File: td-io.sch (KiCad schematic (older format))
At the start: 99 parts, among them J1 USB_A, J2 USB_B, J3 JAMMA_Edge, J4 Conn_Coaxial, J5 DB15_Female_HighDensity, J6 Conn_02x04_Top_Bottom, J7 Conn_02x17_Odd_Even, J8 Conn_Coaxial, Q1 FDS6930B, Q2 FDS6930B, Q3 FDS6930B, SW1 SW_DIP_x02, U1 LM4950TS, U10 Pico, U11 TL081, U12 CPC1017N, U2 SP3481CN, U3 AD813, U4 74LS86, U5 AT24CS01-SSHM, U6 74LV166, U7 TPS568230, U8 74LV166, U9 74LV166

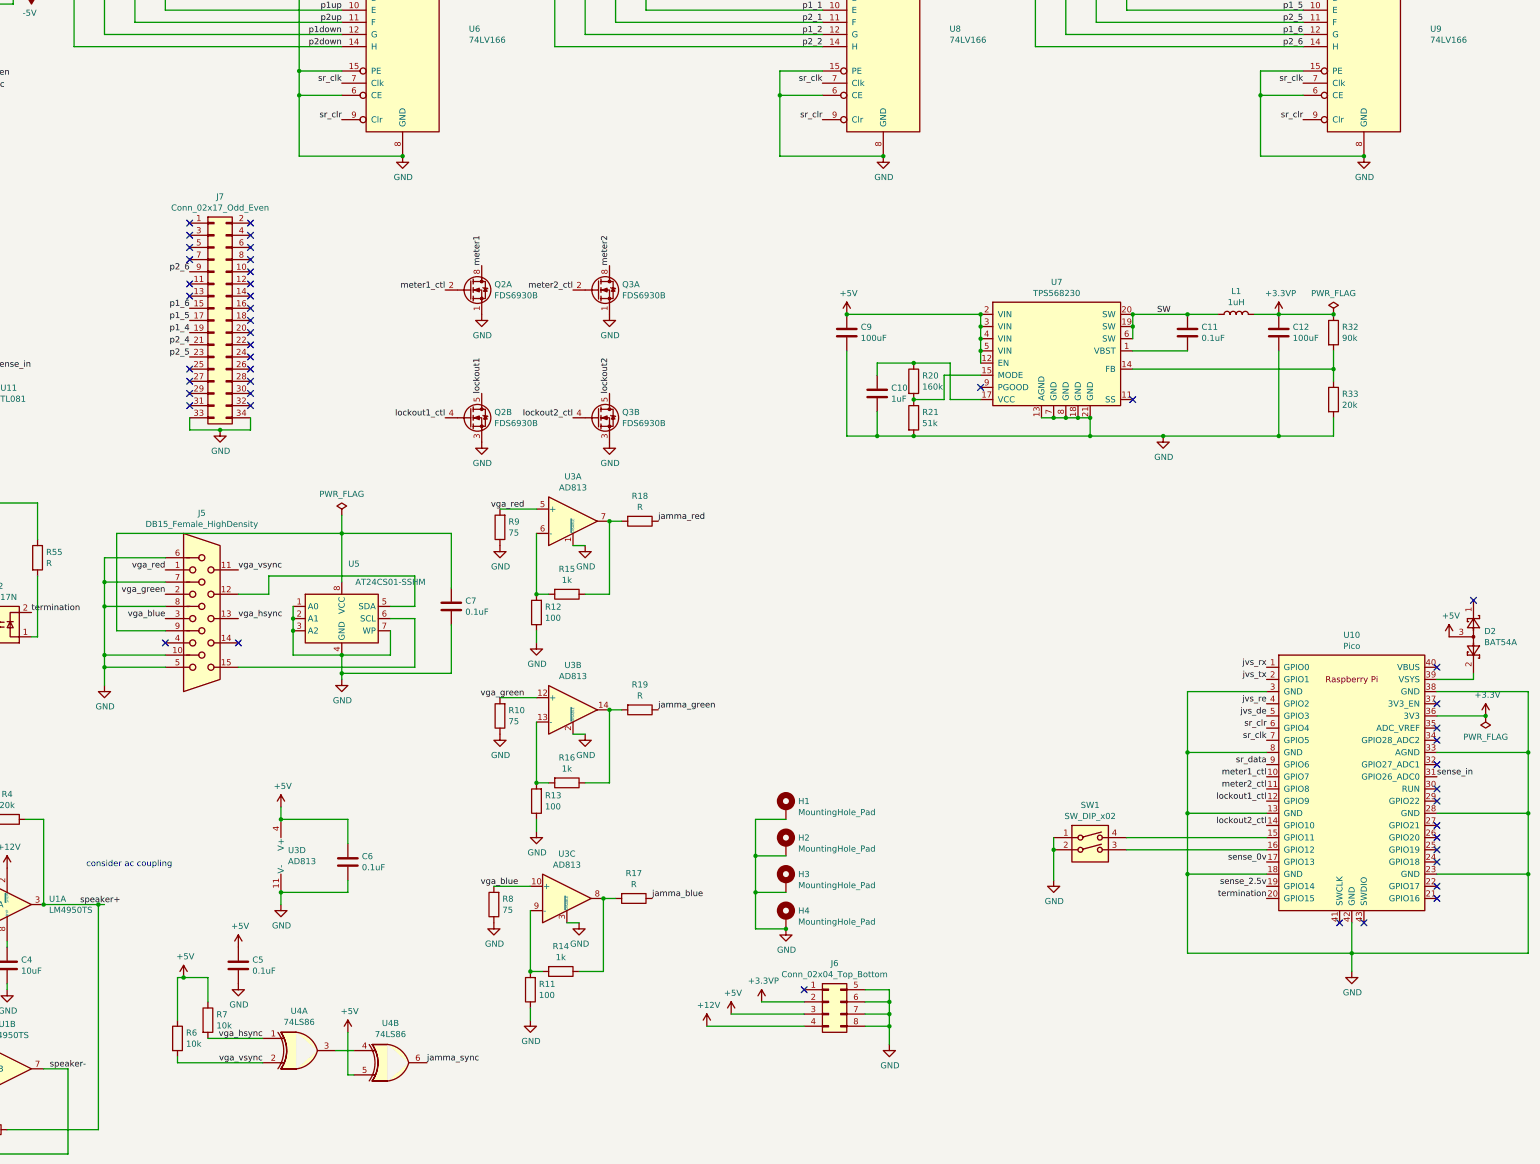
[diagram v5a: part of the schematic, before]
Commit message: More layout fixes
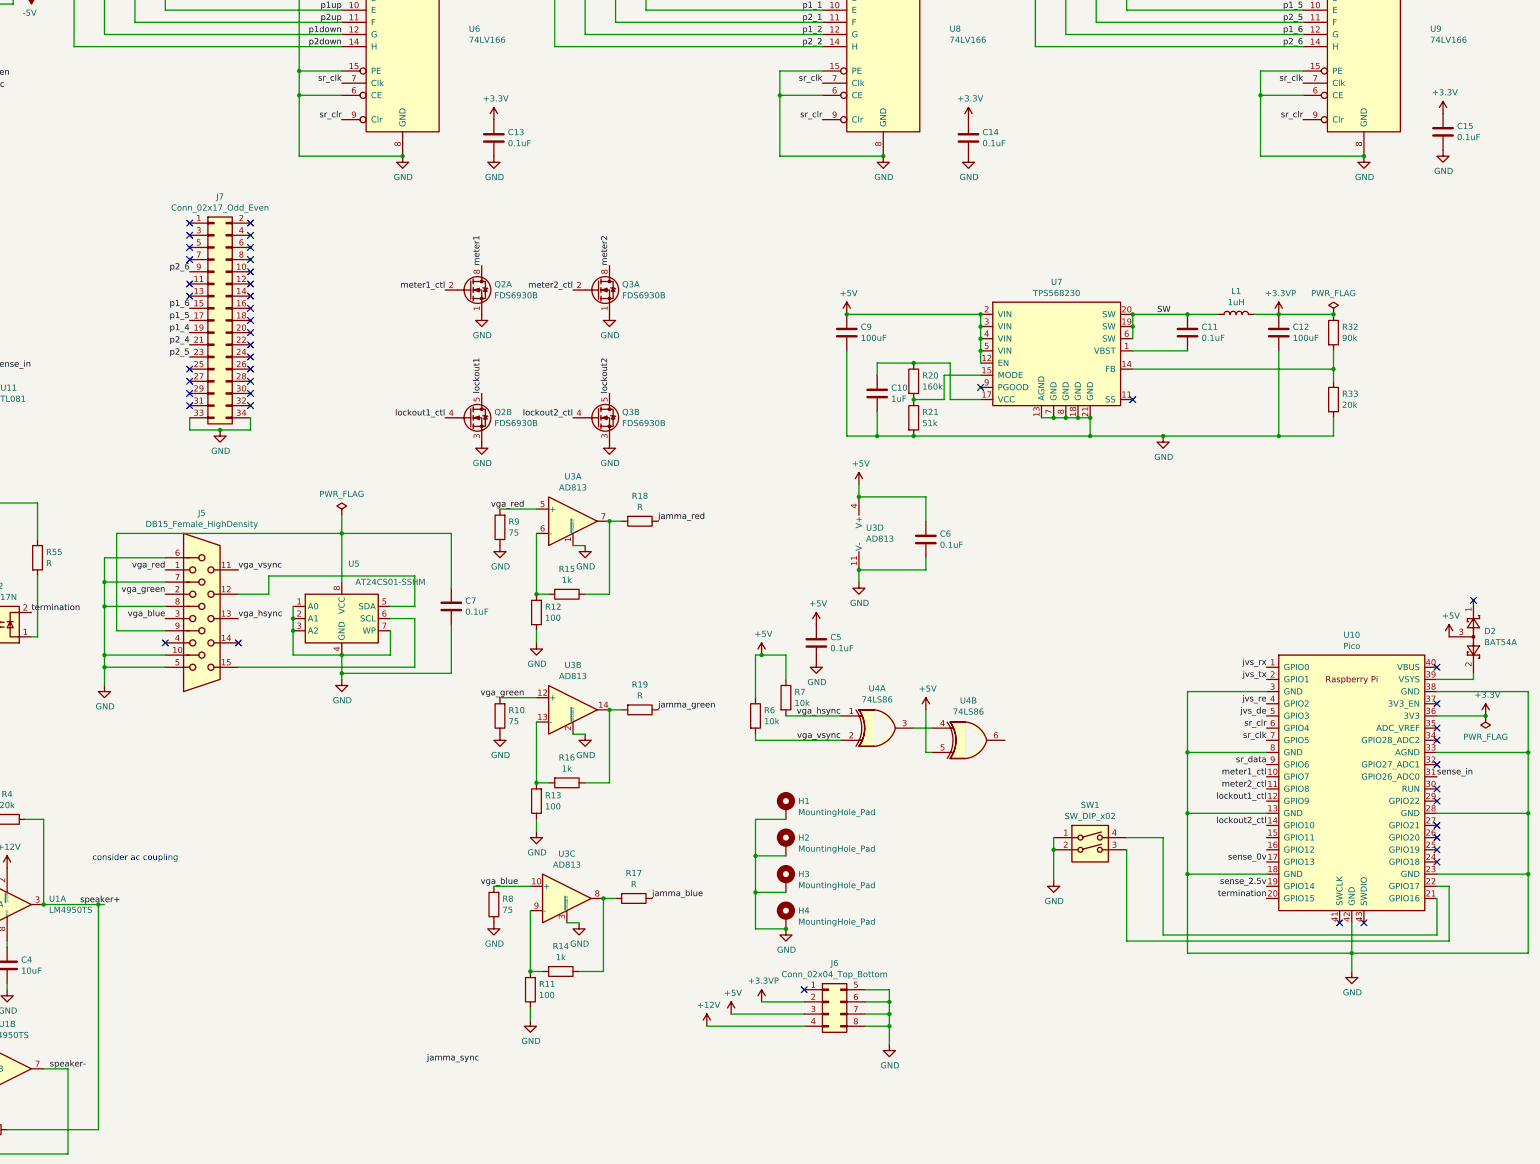
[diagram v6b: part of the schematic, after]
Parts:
- added C13, C14, C15: 0.1uF, Capacitor_SMD:C_0805_2012Metric, symbol Device:C
- R50, R51, R52, R53, R54, R55: footprint (none) -> Resistor_SMD:R_0805_2012Metric
- U11: footprint (none) -> Package_SO:SOIC-8_3.9x4.9mm_P1.27mm
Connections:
- net +3V3: now also C13.1, C14.1, C15.1
- net GND: now also C13.2, C14.2, C15.2
- net jamma_sync: no longer U4.6
- net at U10.15 (GPIO11): no longer SW1.4
- net at U10.16 (GPIO12): no longer SW1.3
- net at U10.21 (GPIO16): now also SW1.4
- net at U10.22 (GPIO17): now also SW1.3
- no-connect marks 53 -> 51
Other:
- moved on the sheet: C5, C6, R6, R7, U3D, U4A, U4B

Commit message: Switch from 74lv166 to 74lv165
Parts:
- U6, U8, U9: value 74LV166 -> 74LS165; symbol 74xx:74LS166 -> 74xx:74LS165
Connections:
- net GND: now also U6.10 (DS); no longer U6.1 (Ds), U6.6 (CE), U8.6 (CE), U9.6 (CE)
- net c1: now also U6.11 (D0); no longer U6.2 (A)
- net c2: now also U6.12 (D1); no longer U6.3 (B)
- net p1_1: now also U8.3 (D4); no longer U8.10 (E)
- net p1_2: now also U8.5 (D6); no longer U8.12 (G)
- net p1_3: now also U9.11 (D0); no longer U9.2 (A)
- net p1_4: now also U9.13 (D2); no longer U9.4 (C)
- net p1_5: now also U9.3 (D4); no longer U9.10 (E)
- net p1_6: now also U9.5 (D6); no longer U9.12 (G)
- net p1down: now also U6.5 (D6); no longer U6.12 (G)
- net p1left: now also U8.11 (D0); no longer U8.2 (A)
- net p1right: now also U8.13 (D2); no longer U8.4 (C)
- net p1start: now also U6.13 (D2); no longer U6.4 (C)
- net p1up: now also U6.3 (D4); no longer U6.10 (E)
- net p2_1: now also U8.4 (D5); no longer U8.11 (F)
- net p2_2: now also U8.6 (D7); no longer U8.14 (H)
- net p2_3: now also U9.12 (D1); no longer U9.3 (B)
- net p2_4: now also U9.14 (D3); no longer U9.5 (D)
- net p2_5: now also U9.4 (D5); no longer U9.11 (F)
- net p2_6: now also U9.6 (D7); no longer U9.14 (H)
- net p2down: now also U6.6 (D7); no longer U6.14 (H)
- net p2left: now also U8.12 (D1); no longer U8.3 (B)
- net p2right: now also U8.14 (D3); no longer U8.5 (D)
- net p2start: now also U6.14 (D3); no longer U6.5 (D)
- net p2up: now also U6.4 (D5); no longer U6.11 (F)
- net sr_clk: now also U6.2 (CP), U8.2 (CP), U9.2 (CP); no longer U6.7 (Clk), U8.7 (Clk), U9.7 (Clk)
- net sr_clr: now also U6.1 (~PL), U8.1 (~PL), U9.1 (~PL); no longer U6.9 (Clr), U8.9 (Clr), U9.9 (Clr)
- net sr_data: now also U9.9 (Q7); no longer U9.13 (Qh)
- new net: U6.9 (Q7), U8.10 (DS)
- new net: U8.9 (Q7), U9.10 (DS)
- no-connect marks 51 -> 54
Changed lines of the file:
@@
 $EndComp
 $Comp
-L 74xx:74LS166 U6
+L 74xx:74LS165 U6
 U 1 1 601A3120
-P 6700 1900
-F 0 "U6" H 7244 1946 50  0000 L CNN
-F 1 "74LV166" H 7244 1855 50  0000 L CNN
-F 2 "Package_SO:SOIC-16_3.9x9.9mm_P1.27mm" H 6700 1900 50  0001 C CNN
-F 3 "http://www.ti.com/lit/gpn/sn74LS166" H 6700 1900 50  0001 C CNN
-	1    6700 1900
+P 6700 1800
+F 0 "U6" H 7244 1846 50  0000 L CNN
+F 1 "74LS165" H 7244 1755 50  0000 L CNN
+F 2 "Package_SO:SOIC-16_3.9x9.9mm_P1.27mm" H 6700 1800 50  0001 C CNN
+F 3 "https://www.ti.com/lit/ds/symlink/sn74ls165a.pdf" H 6700 1800 50  0001 C CNN
+	1    6700 1800
 	1    0    0    -1
 $EndComp
@@
 	1    0    0    -1
 $EndComp
-Text Label 6200 2600 2    50   ~ 0
+Text Label 6200 2200 2    50   ~ 0
 sr_clr
-Text Label 6200 2300 2    50   ~ 0
+Text Label 6200 2400 2    50   ~ 0
 sr_clk
 Wire Wire Line
-	6700 2900 5850 2900
-Wire Wire Line
-	5850 2900 5850 2400
-Wire Wire Line
-	5850 2400 6200 2400
-Connection ~ 6700 2900
-Wire Wire Line
-	5850 2400 5850 2200
-Wire Wire Line
-	5850 2200 6200 2200
-Connection ~ 5850 2400
+	6700 2900 6200 2900
 $Comp
 L Connector_Generic:Conn_02x17_Odd_Even J7
@@
 $EndComp
 Wire Wire Line
-	5850 2200 5850 1200
-Wire Wire Line
 	5850 1200 6200 1200
-Connection ~ 5850 2200
 Wire Wire Line
 	6200 1300 5750 1300
@@
 	4850 800  5000 800
 $Comp
-L 74xx:74LS166 U8
+L 74xx:74LS165 U8
 U 1 1 6055CE93
-P 10650 1900
-F 0 "U8" H 11194 1946 50  0000 L CNN
-F 1 "74LV166" H 11194 1855 50  0000 L CNN
-F 2 "Package_SO:SOIC-16_3.9x9.9mm_P1.27mm" H 10650 1900 50  0001 C CNN
-F 3 "http://www.ti.com/lit/gpn/sn74LS166" H 10650 1900 50  0001 C CNN
-	1    10650 1900
+P 10650 1800
+F 0 "U8" H 11194 1846 50  0000 L CNN
+F 1 "74LS165" H 11194 1755 50  0000 L CNN
+F 2 "Package_SO:SOIC-16_3.9x9.9mm_P1.27mm" H 10650 1800 50  0001 C CNN
+F 3 "https://www.ti.com/lit/ds/symlink/sn74ls165a.pdf" H 10650 1800 50  0001 C CNN
+	1    10650 1800
 	1    0    0    -1
 $EndComp
@@
 	1    0    0    -1
 $EndComp
-Text Label 10150 2600 2    50   ~ 0
+Text Label 10150 2200 2    50   ~ 0
 sr_clr
-Text Label 10150 2300 2    50   ~ 0
+Text Label 10150 2400 2    50   ~ 0
 sr_clk
-Wire Wire Line
-	10650 2900 9800 2900
-Wire Wire Line
-	9800 2900 9800 2400
-Wire Wire Line
-	9800 2400 10150 2400
-Connection ~ 10650 2900
-Wire Wire Line
-	9800 2400 9800 2200
-Wire Wire Line
-	9800 2200 10150 2200
-Connection ~ 9800 2400
 $Comp
 L Device:R R34
@@
 	8800 800  8950 800
 $Comp
-L 74xx:74LS166 U9
-U 1 1 605892D9
-P 14600 1900
-F 0 "U9" H 15144 1946 50  0000 L CNN
-F 1 "74LV166" H 15144 1855 50  0000 L CNN
-F 2 "Package_SO:SOIC-16_3.9x9.9mm_P1.27mm" H 14600 1900 50  0001 C CNN
-F 3 "http://www.ti.com/lit/gpn/sn74LS166" H 14600 1900 50  0001 C CNN
-	1    14600 1900
-	1    0    0    -1
-$EndComp
-$Comp
 L power:+3.3V #PWR012
 U 1 1 605892DF
@@
 	1    0    0    -1
 $EndComp
-Text Label 14100 2600 2    50   ~ 0
+Text Label 14100 2200 2    50   ~ 0
 sr_clr
-Text Label 14100 2300 2    50   ~ 0
+Text Label 14100 2400 2    50   ~ 0
 sr_clk
-Wire Wire Line
-	14600 2900 13750 2900
-Wire Wire Line
-	13750 2900 13750 2400
-Wire Wire Line
-	13750 2400 14100 2400
-Connection ~ 14600 2900
-Wire Wire Line
-	13750 2400 13750 2200
-Wire Wire Line
-	13750 2200 14100 2200
-Connection ~ 13750 2400
 $Comp
 L Device:R R42
@@
 $EndComp
 Wire Wire Line
-	14100 1300 13650 1300
-Wire Wire Line
 	13650 1300 13650 1100
 Wire Wire Line
-	14100 1400 13400 1400
-Wire Wire Line
 	13400 1400 13400 1100
 Wire Wire Line
-	14100 1500 13150 1500
-Wire Wire Line
 	13150 1500 13150 1100
 Wire Wire Line
-	14100 1600 12900 1600
-Wire Wire Line
 	12900 1600 12900 1100
 Wire Wire Line
-	14100 1700 12650 1700
-Wire Wire Line
 	12650 1700 12650 1100
 Wire Wire Line
-	14100 1800 12400 1800
-Wire Wire Line
 	12400 1800 12400 1100
 Wire Wire Line
-	14100 1900 12150 1900
-Wire Wire Line
 	12150 1900 12150 1100
-Wire Wire Line
-	14100 2000 11900 2000
 Wire Wire Line
 	11900 2000 11900 1100
@@
 Wire Wire Line
 	12750 800  12900 800
-Wire Wire Line
-	11150 1200 14100 1200
 Wire Wire Line
 	10150 1200 7200 1200
@@
 Wire Wire Line
 	15300 8900 15200 8900
+Wire Wire Line
+	5850 1200 5850 2900
+Wire Wire Line
+	6200 2500 6200 2900
+Connection ~ 6200 2900
+Wire Wire Line
+	6200 2900 5850 2900
+Wire Wire Line
+	6700 2800 6700 2900
+Connection ~ 6700 2900
+NoConn ~ 7200 1300
+Wire Wire Line
+	10650 2900 10650 2800
+Wire Wire Line
+	10150 2500 10150 2900
+Wire Wire Line
+	10150 2900 10650 2900
+Connection ~ 10650 2900
+Wire Wire Line
+	14100 2000 11900 2000
+Wire Wire Line
+	14100 1900 12150 1900
+Wire Wire Line
+	14100 1800 12400 1800
+Wire Wire Line
+	14100 1700 12650 1700
+Wire Wire Line
+	14100 1600 12900 1600
+Wire Wire Line
+	14100 1500 13150 1500
+Wire Wire Line
+	14100 1400 13400 1400
+Wire Wire Line
+	14100 1300 13650 1300
+Wire Wire Line
+	11150 1200 14100 1200
+$Comp
+L 74xx:74LS165 U9
+U 1 1 605892D9
+P 14600 1800
+F 0 "U9" H 15144 1846 50  0000 L CNN
+F 1 "74LS165" H 15144 1755 50  0000 L CNN
+F 2 "Package_SO:SOIC-16_3.9x9.9mm_P1.27mm" H 14600 1800 50  0001 C CNN
+F 3 "https://www.ti.com/lit/ds/symlink/sn74ls165a.pdf" H 14600 1800 50  0001 C CNN
+	1    14600 1800
+	1    0    0    -1
+$EndComp
+Wire Wire Line
+	14600 2800 14600 2900
+Wire Wire Line
+	14100 2500 14100 2900
+Wire Wire Line
+	14100 2900 14600 2900
+Connection ~ 14600 2900
+NoConn ~ 15100 1300
+NoConn ~ 11150 1300
 $EndSCHEMATC

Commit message: Add service/test/tilt
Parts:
- added C16: 0.1uF, Capacitor_SMD:C_0805_2012Metric, symbol Device:C
- added R56, R57, R58: 10k, Resistor_SMD:R_0805_2012Metric, symbol Device:R
- added U13: 74LS165, Package_SO:SOIC-16_3.9x9.9mm_P1.27mm, symbol 74xx:74LS165
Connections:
- net +3V3: now also C16.1, R56.1, R57.1, R58.1, U13.14 (D3), U13.16 (VCC), U13.3 (D4), U13.4 (D5), U13.5 (D6), U13.6 (D7)
- net GND: now also C16.2, U13.10 (DS), U13.15 (~CE), U13.8 (GND); no longer U6.10 (DS)
- net sr_clk: now also U13.2 (CP)
- net sr_clr: now also U13.1 (~PL)
- net test: now reaches J3.15 (Test)
- net test: now also R57.2, U13.12 (D1)
- net service: now reaches J3.R (Service)
- net service: now also R58.2, U13.11 (D0)
- net tilt: now reaches J3.S (Tilt)
- net tilt: now also R56.2, U13.13 (D2)
- new net: U13.9 (Q7), U6.10 (DS)
- no-connect marks 54 -> 55
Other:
- moved on the sheet: C13, C14, C15, R22, R23, R24, R27, R28, R29, R30, R31, R34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
